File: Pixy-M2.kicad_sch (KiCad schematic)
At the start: 44 parts, among them J1 USB_C_Receptacle_USB2.0_14P, J2 Conn_01x22_Pin, J3 Conn_01x22_Pin, SW1 SW_Push, SW2 SW_Push, U1 ESP32-S3-WROOM-1-N16, U2 USBLC6-2SC6, U3 AP63203WU

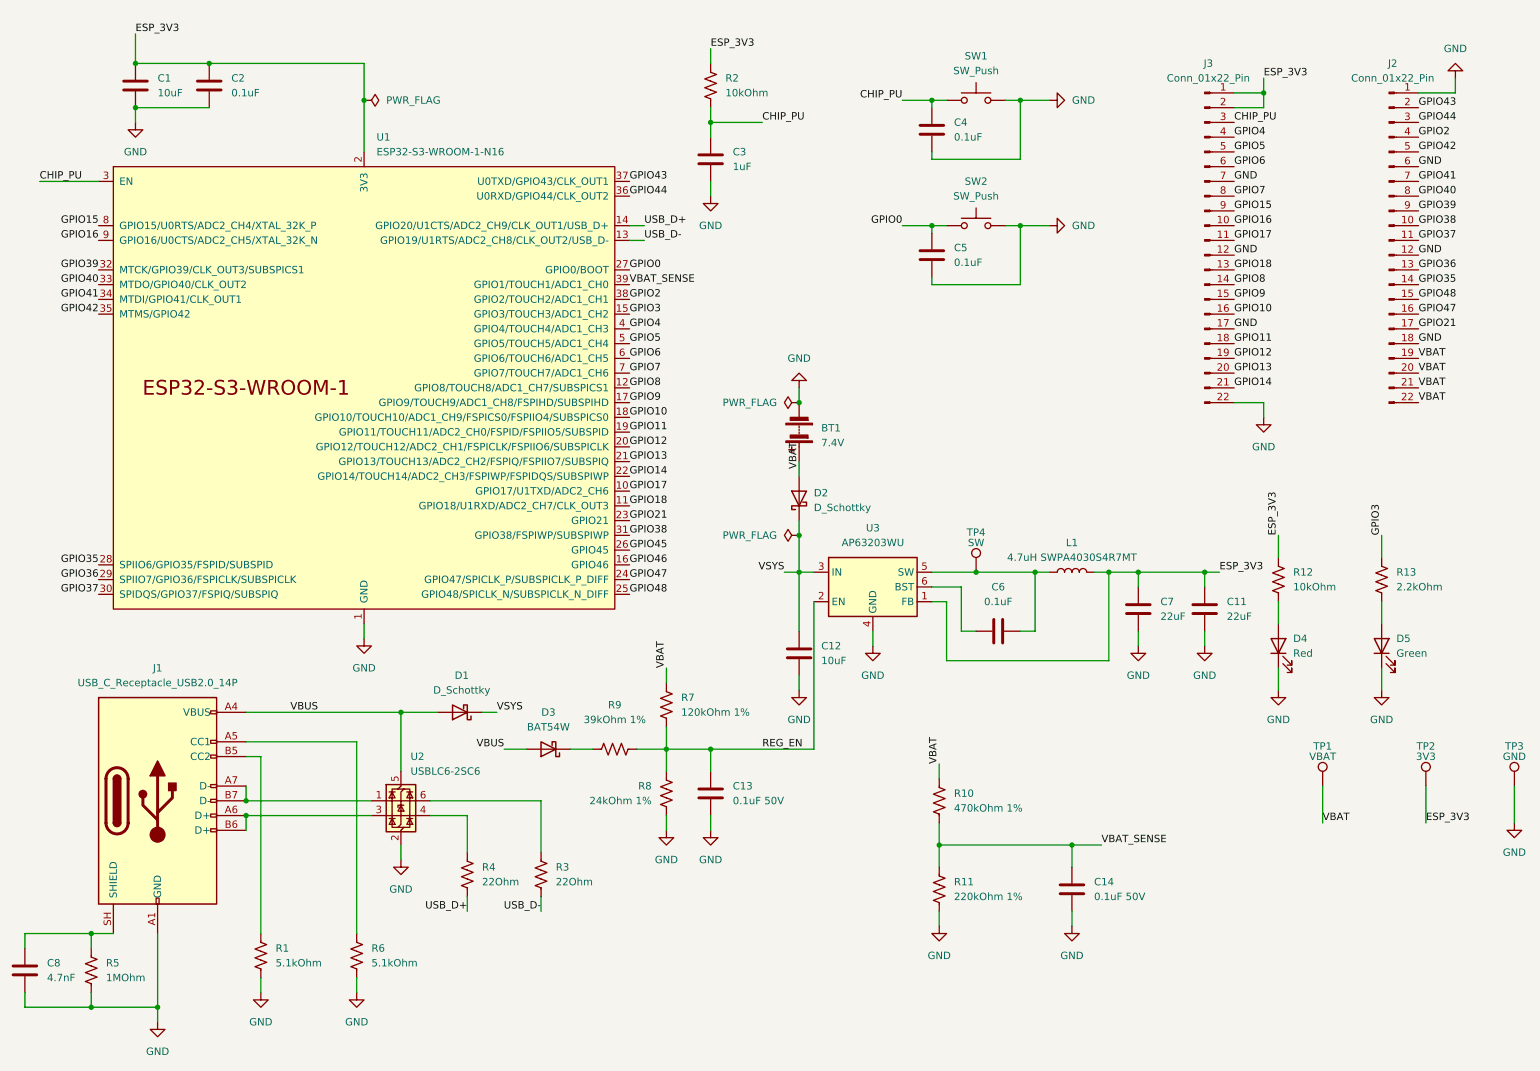
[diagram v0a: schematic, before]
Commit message: Add battery power switch, input fuses and TVS (issue 7)
The battery previously fed the regulator and daughterboard directly, with
no power switch or fuse. The UVLO and battery-sense dividers also remained
connected to the pack, drawing about 70uA even when the regulator stopped.
USB VBUS likewise had no board-level fuse, and the shared motor supply had
no transient clamp.

Add six components to the schematic:

- F1: Littelfuse 2920L300/15DR battery PPTC, provisionally 3A hold / 5A trip
  at 20C, rated for 15V, in a 2920 footprint.
- Q1: AO4407A P-channel MOSFET load switch, with source pins 1-3 connected
  to VBAT_FUSED and drain pins 5-8 connected to the existing VBAT net.
- R14: 100k gate-to-source pull-up so Q1 defaults off.
- SW3: C&K JS102011SAQN slide switch controlling Q1's gate, keeping motor
  current out of the switch contacts. Pins 2-3 select ON; pins 2-1 select
  OFF, with pin 1 intentionally marked no-connect.
- F2: Bourns MF-MSMF050-2 USB PPTC, 500mA hold / 1A trip at 23C, rated for
  15V, ahead of D1, the D3/R9 enable path and U2's VBUS clamp reference.
- D6: SMBJ9.0A-E3/52 unidirectional TVS across switched VBAT and GND, with
  its cathode on VBAT and a 9V standoff above the 8.4V full-pack voltage.

Introduce VBAT_RAW and VBAT_FUSED upstream of the load switch. Preserve
VBAT and VBUS for the protected downstream rails, and retain every
existing daughterboard pin assignment. Both battery dividers, TP1 and
J2.19-22 are now downstream of Q1. USB can still power the controller
while the battery switch is off.

Specify the new protection and switching parts with matching footprints,
MPNs and manufacturer datasheets. Q1 uses the stock IRF7404 symbol for
its compatible SO-8 pin map; its fitted part, Value, MPN and Datasheet
all specify AO4407A.

Update CLAUDE.md with the extracted net map, circuit operation, layout
requirements and remaining design checks. Document MOSFET off-state
leakage, the body-diode return path, USB bias through the EN network,
and th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
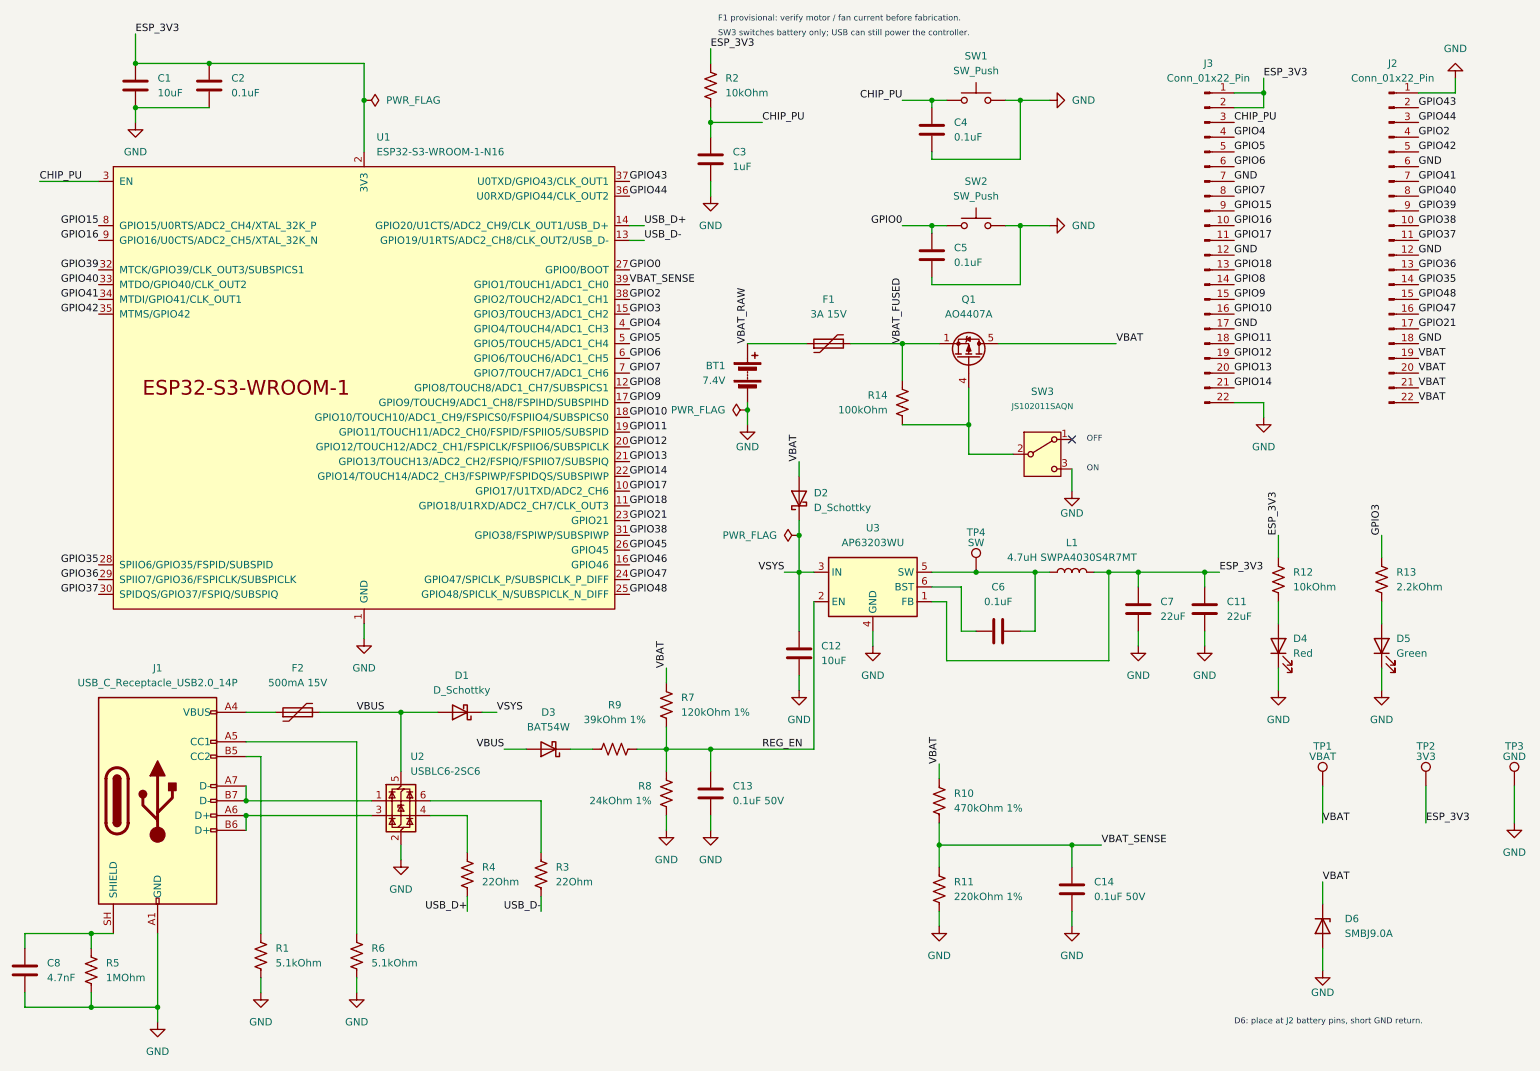
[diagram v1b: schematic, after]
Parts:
- added D6: SMBJ9.0A, Diode_SMD:D_SMB, symbol Device:D_Zener
- added F1: 3A 15V, Fuse:Fuse_2920_7451Metric, symbol Device:Polyfuse
- added F2: 500mA 15V, Fuse:Fuse_1812_4532Metric, symbol Device:Polyfuse
- added Q1: AO4407A, Package_SO:SOIC-8_3.9x4.9mm_P1.27mm, symbol Transistor_FET:IRF7404
- added R14: 100kOhm, Resistor_SMD:R_0805_2012Metric, symbol Device:R_US
- added SW3: JS102011SAQN, Button_Switch_SMD:SW_SPDT_CK_JS102011SAQN, symbol Switch:SW_SPDT
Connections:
- net GND: now also D6.2 (A), SW3.3 (C)
- net VBAT: now also D6.1 (K), Q1.5 (D), Q1.6 (D), Q1.7 (D), Q1.8 (D); no longer BT1.1 (+)
- net VBUS: now also F2.2; no longer J1.A4 (VBUS), J1.A9 (VBUS), J1.B4 (VBUS), J1.B9 (VBUS)
- new net: Q1.4 (G), R14.2, SW3.2 (B)
- new net: F2.1, J1.A4 (VBUS), J1.A9 (VBUS), J1.B4 (VBUS), J1.B9 (VBUS)
- new net VBAT_FUSED: F1.2, Q1.1 (S), Q1.2 (S), Q1.3 (S), R14.1
- new net VBAT_RAW: BT1.1 (+), F1.1
- no-connect marks 0 -> 1
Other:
- note added: "D6: place at J2 battery pins, short GND return."
- note added: "F1 provisional: verify motor / fan current before fabrication."
- note added: "OFF"
- note added: "ON"
- note added: "SW3 switches battery only; USB can still power the controller."
- moved on the sheet: BT1
